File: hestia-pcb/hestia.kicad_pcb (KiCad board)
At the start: 4 copper layers, 90.2 x 95.9 mm, 181 parts, among them J1 Serial Connector, J12 B2B-ZR, J13 B2B-ZR, J14 B2B-ZR, J15 B2B-ZR, J16 B2B-ZR, J2 i2c connector, J3 ESQ-126-39-G-D, J4 ESQ-126-39-G-D, J5 VREF+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

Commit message: shift template designator/value locations for SRP5030C footprint in library. Update hestia PCB with SRP5030C footprint for L2 on buck regulator. change D7 footprint from SOT23 to smaller SOT-323 as per diode on BOM.
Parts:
- D7: footprint Package_TO_SOT_SMD:SOT-23 -> Package_TO_SOT_SMD:SOT-323_SC-70_Handsoldering
- L2: footprint Inductor_SMD:L_Coilcraft_LPS5030 -> Hestia:SRP5030C
- TH1, TH2, TH3, TH4, TH5, TH6: value Thermistor NTC 10K 3630K -> Thermistor NTC 10K 3610K
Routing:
- net +3.3V: track 114.3 -> 115.0 mm

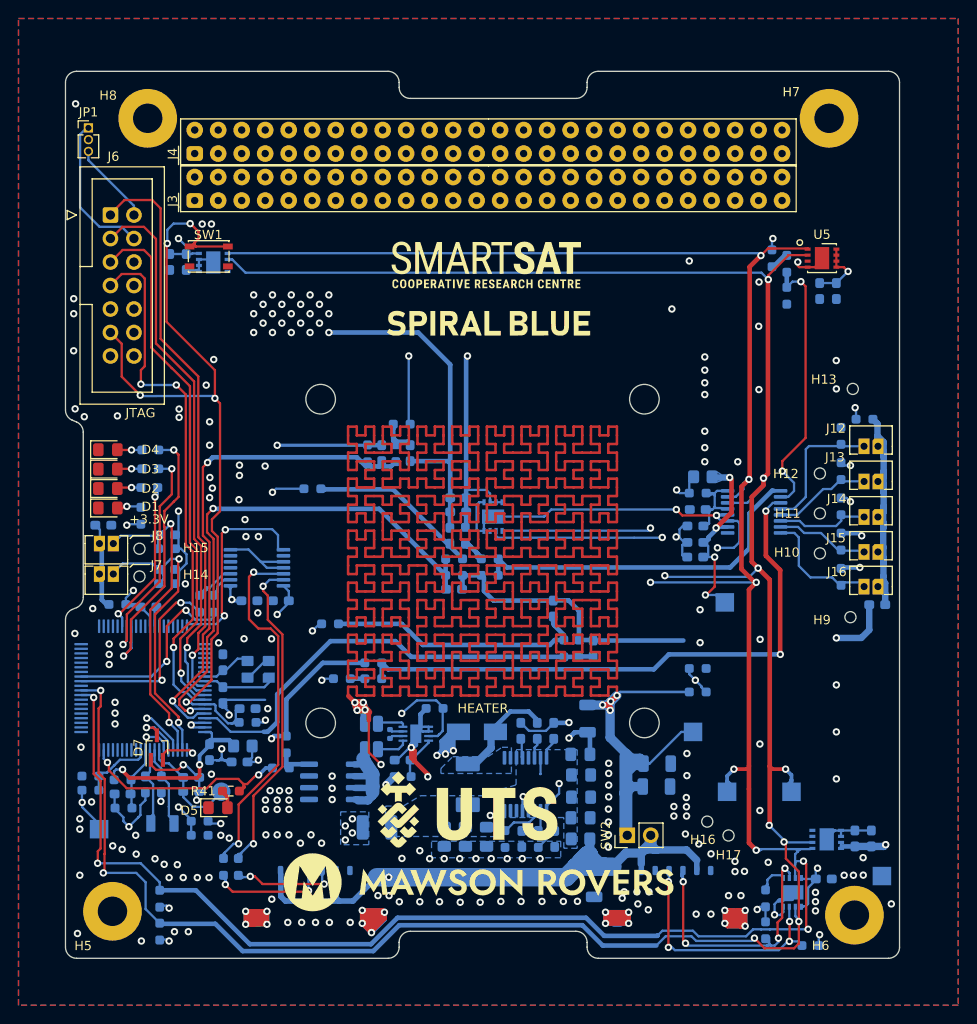
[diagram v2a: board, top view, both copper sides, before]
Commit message: added new themal switch footprint to hestia lib. Added 3 wire restraint hole footprints -> 1.2mm, 1.8mm and 1.9mm. Change adc wire restraint holes (H9 to H13) to 1.8mm. Change uC wire restraint holes(H14 & H15) to 1.8mm & moved H14 & H15 designators. Change thermal switch wire restraint holes (H16 & H17) to 1.9mm & also shifted hole coords left 0.2mm & moved H16 & H17 designators. Change thermal switch footprint to new footprint with thruhole pads to 1.2mm dia hole as well as with increased pad distance. Thicken VCC traces to thermal switch - have to revisit to satisfy DRC - probably change multiple traces to signal polygon. Added two GND vias for extra GND stitching off J2. ToDo -Resolve DRC issues. Some padd may need extra signal spurs to pads - just manually adding a trace to the pads may satisfy the DRC requirement
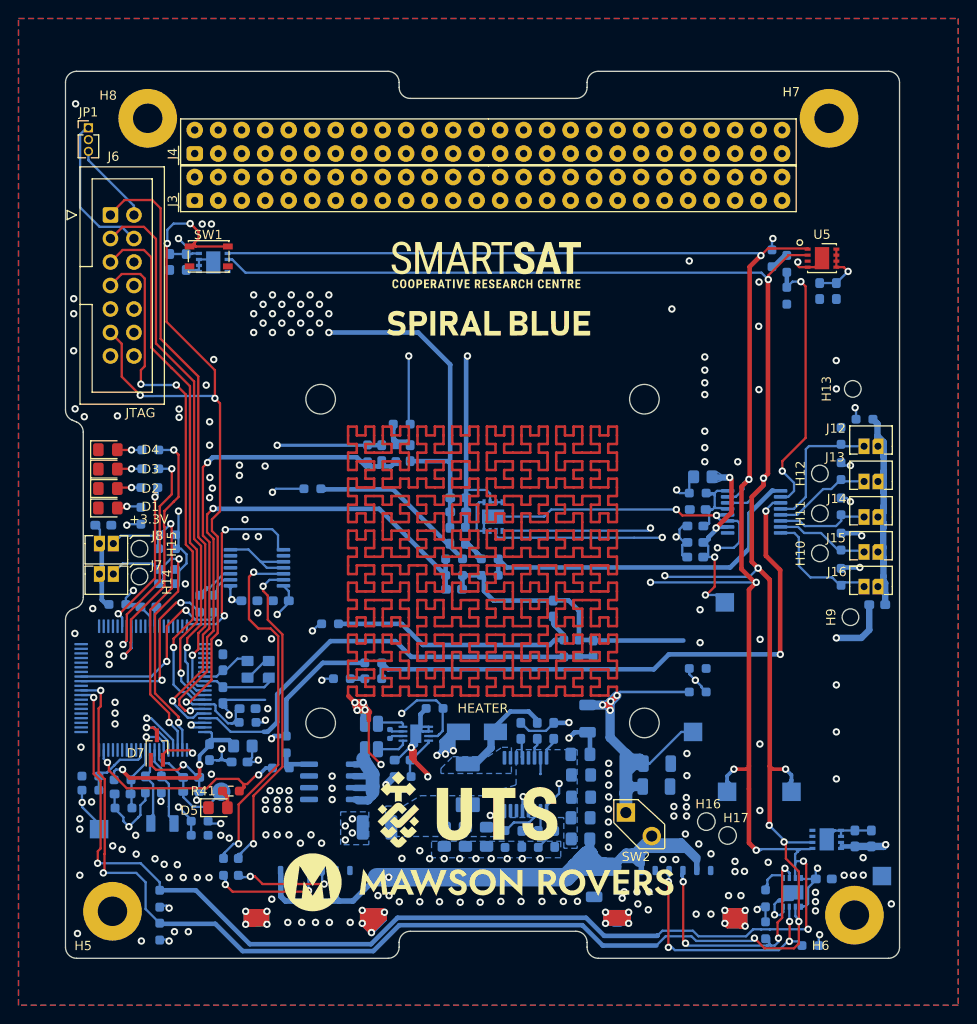
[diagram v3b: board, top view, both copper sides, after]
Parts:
- H10, H11, H12, H13, H14, H15, H9: footprint Hestia:Wire_Restraint_Hole -> Hestia:Wire_Restraint_Hole_1.8mm
- H16, H17: footprint Hestia:Wire_Restraint_Hole -> Hestia:Wire_Restraint_Hole_1.9mm
- SW2: footprint Connector_PinHeader_2.54mm:PinHeader_1x02_P2.54mm_Vertical -> Hestia:Thermal Switch
- moved SW2 2.46 mm to (162.2, 141.2), turned to 0 degrees
- moved H16 0.10 mm to (170.9, 142.2)
- moved H17 0.10 mm to (173.2, 143.7)
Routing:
- net VCC: track 94.3 -> 109.7 mm
- net /heater/Heater high: track 1006.0 -> 1003.4 mm
- net GND: vias 223 -> 225

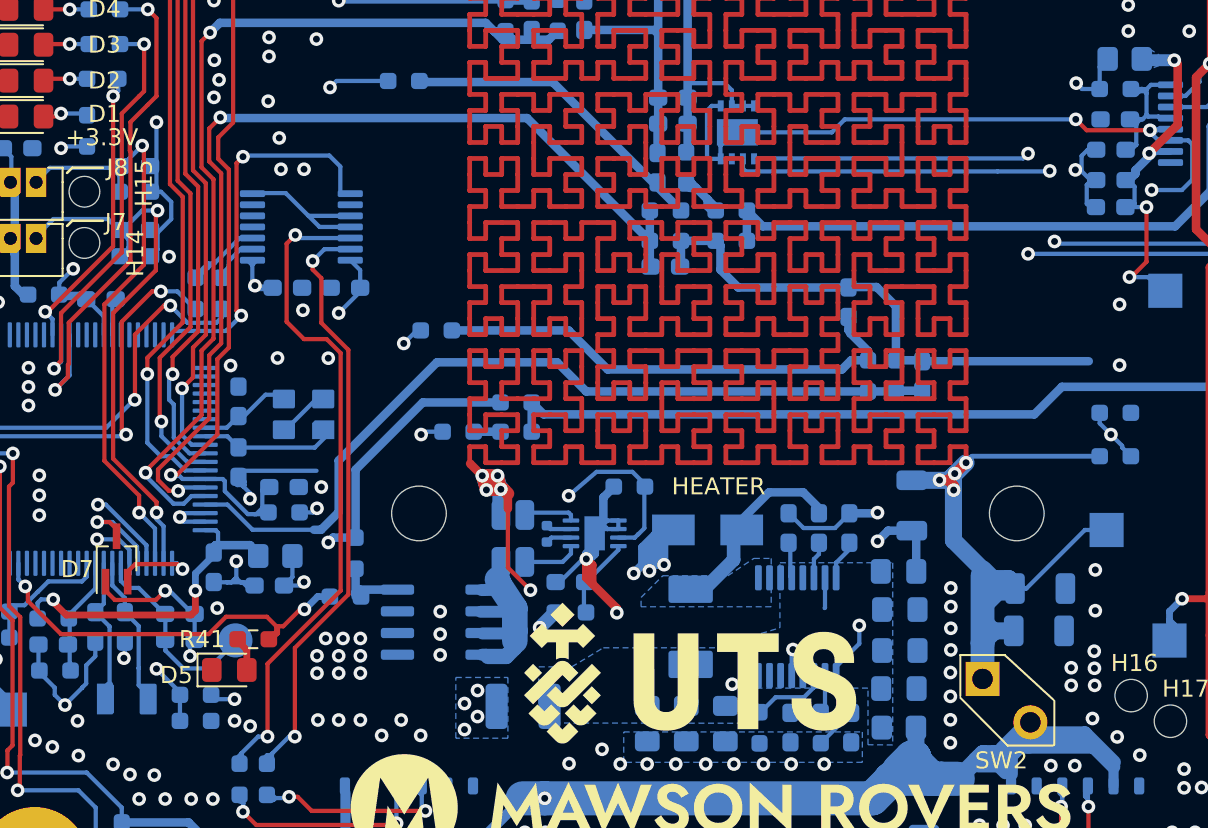
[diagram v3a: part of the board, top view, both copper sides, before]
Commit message: Moved U1 designator due to DRC violation. Moved C1 designator due to DRC violation after SW2 footprint was previously changed and shifted. Moved C26 designator due to DRC violation after SW2 footprint was previously changed and shifted. Changed R42 desgnator height to 0.8mm due to new DRC violation for minimum. Previous height was 0.6mm. Moved GND via near new thermal switch pads to satisfy DRC clearance violation. Move GND trace near D7 pin 2 to satisfy DRC clearance violation. Added PCB trace at C24 pin2 to satisfy ground polygon minimum thermal trace spoke to pad of 2 spokes.
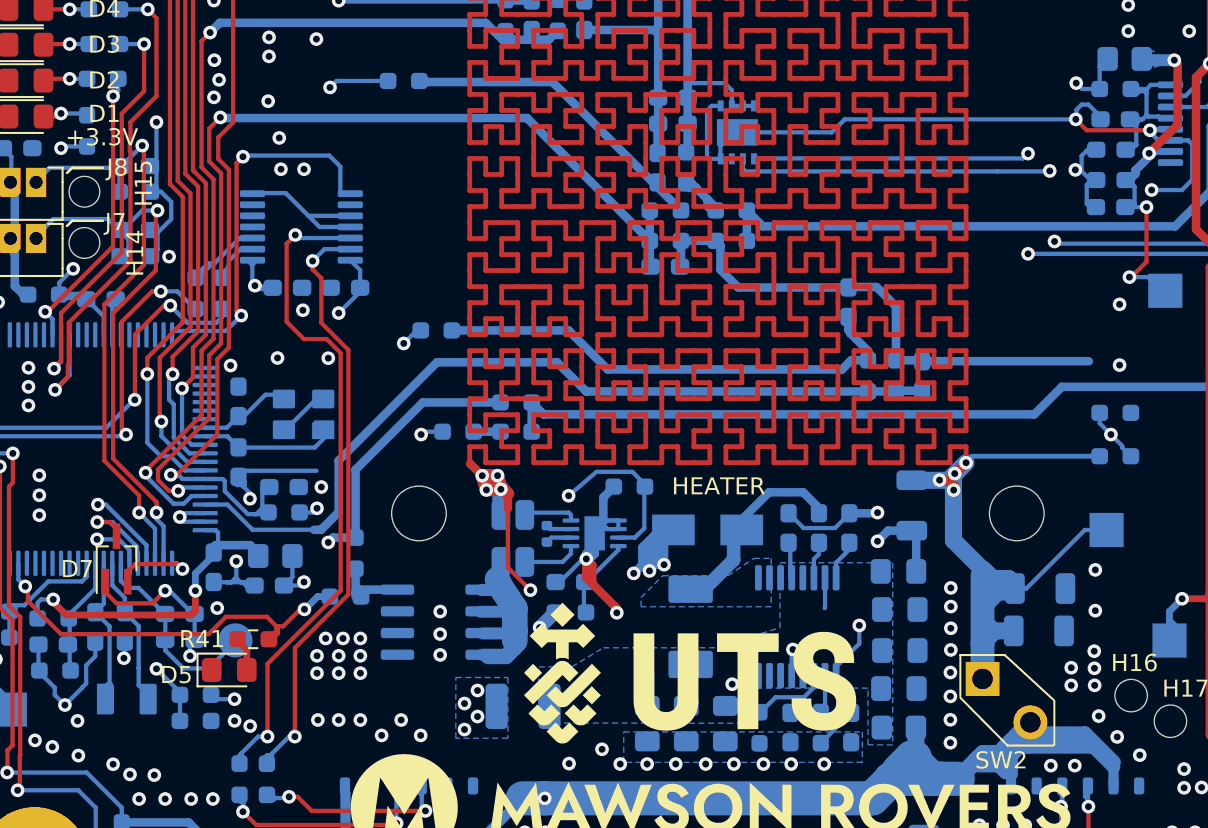
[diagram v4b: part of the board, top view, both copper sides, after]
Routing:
- net GND: track 282.2 -> 285.0 mm
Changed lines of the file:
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@@
     (property "ki_keywords" "cap capacitor")
     (attr smd)
-    (fp_text reference "C1" (at 4.5148 -0.0508) (layer "B.SilkS")
+    (fp_text reference "C1" (at 4.5148 1.2123) (layer "B.SilkS")
         (effects (font (size 1 1) (thickness 0.15)) (justify mirror))
     )
@@
     (property "ki_keywords" "cap capacitor")
     (attr smd)
-    (fp_text reference "C26" (at 4.677652 0.1686) (layer "B.SilkS")
+    (fp_text reference "C26" (at 4.677652 0.0383) (layer "B.SilkS")
         (effects (font (size 1 1) (thickness 0.15)) (justify mirror))
     )
@@
     (property "Type" "SMD")
     (attr smd)
-    (fp_text reference "U1" (at -3.090248 3.3518 -90) (layer "B.SilkS")
-        (effects (font (size 1 1) (thickness 0.15)) (justify mirror))
+    (fp_text reference "U1" (at -3.165248 3.3518 -90) (layer "B.SilkS")
+        (effects (font (size 0.8 0.8) (thickness 0.15)) (justify mirror))
     )
     (fp_text value "LM2655MTC-3.3/NOPB" (at 0 -3.45 90) (layer "B.Fab")
@@
     (attr smd)
     (fp_text reference "R42" (at 2.509116 -1.001059) (layer "B.SilkS")
-        (effects (font (size 0.6 0.6) (thickness 0.1)) (justify mirror))
+        (effects (font (size 0.8 0.8) (thickness 0.15) bold) (justify mirror))
     )
     (fp_text value "499R 0.1% 1/16W" (at 0 -1.16 90) (layer "B.Fab")
@@
   (gr_line (start 114.5814 118.2231) (end 115.2314 118.2231)
     (stroke (width 0.15) (type solid)) (layer "B.SilkS"))
-  (gr_line (start 160.9814 141.6231) (end 159.3314 141.6231)
-    (stroke (width 0.15) (type solid)) (layer "B.SilkS"))
   (gr_circle (center 181.9814 152.0231) (end 182.1314 152.1231)
     (stroke (width 0.15) (type solid)) (fill none) (layer "B.SilkS"))
@@
   (gr_line (start 115.216417 140.008421) (end 115.18482 139.713522)
     (stroke (width 0.15) (type solid)) (layer "B.SilkS"))
+  (gr_line (start 159.8814 142.9231) (end 160.9814 143.0231)
+    (stroke (width 0.15) (type default)) (layer "B.SilkS"))
   (gr_circle (center 126.3814 140.4231) (end 126.3814 140.1231)
     (stroke (width 0.15) (type solid)) (fill none) (layer "B.SilkS"))
@@
   (gr_line (start 160.4814 137.4731) (end 159.3814 137.4731)
     (stroke (width 0.15) (type solid)) (layer "B.SilkS"))
-  (gr_line (start 136.276671 130.6758) (end 136.613698 131.065488)
+  (gr_line (start 136.2814 130.7231) (end 136.613698 131.065488)
     (stroke (width 0.1) (type solid)) (layer "B.SilkS"))
   (gr_circle (center 181.3564 145.3731) (end 181.4814 145.5231)
@@
   (gr_line (start 136.613698 131.697414) (end 136.535813 131.615432)
     (stroke (width 0.1) (type solid)) (layer "B.SilkS"))
+  (gr_line (start 159.8814 142.9231) (end 159.3814 142.3231)
+    (stroke (width 0.15) (type default)) (layer "B.SilkS"))
   (gr_line (start 106.0577 140.0455) (end 106.0577 140.1852)
     (stroke (width 0.15) (type solid)) (layer "B.SilkS"))
@@
   (segment (start 168.2771 109.1231) (end 167.64 108.486) (width 0.25) (layer "F.Cu") (net 102))
   (segment (start 139.3314 135.6731) (end 138.9814 135.3231) (width 0.5) (layer "F.Cu") (net 102))
+  (segment (start 111.4814 136.8231) (end 113.5854 136.8231) (width 0.25) (layer "F.Cu") (net 102))
   (segment (start 181.838 82.283) (end 182.5977 82.283) (width 0.25) (layer "F.Cu") (net 102))
   (segment (start 140.769928 137.37548) (end 140.769928 137.111628) (width 0.5) (layer "F.Cu") (net 102))
+  (segment (start 110.7814 135.4106) (end 110.7814 136.1231) (width 0.25) (layer "F.Cu") (net 102))
   (segment (start 171.9814 109.1231) (end 168.2771 109.1231) (width 0.25) (layer "F.Cu") (net 102))
   (segment (start 183.4134 81.4673) (end 183.4134 81.3207) (width 0.25) (layer "F.Cu") (net 102))
   (segment (start 139.3314 134.5731) (end 139.3314 135.6731) (width 0.5) (layer "F.Cu") (net 102))
-  (segment (start 110.7814 135.4106) (end 110.7814 136.0231) (width 0.25) (layer "F.Cu") (net 102))
   (segment (start 138.9814 134.2231) (end 139.3314 134.5731) (width 0.5) (layer "F.Cu") (net 102))
   (segment (start 182.5977 82.283) (end 183.4134 81.4673) (width 0.25) (layer "F.Cu") (net 102))
-  (segment (start 111.3814 136.6231) (end 113.7854 136.6231) (width 0.25) (layer "F.Cu") (net 102))
   (segment (start 181.838 82.283) (end 180.9213 82.283) (width 0.25) (layer "F.Cu") (net 102))
   (segment (start 140.769928 137.111628) (end 139.3314 135.6731) (width 0.5) (layer "F.Cu") (net 102))
-  (segment (start 113.7854 136.6231) (end 114.3254 136.0831) (width 0.25) (layer "F.Cu") (net 102))
-  (segment (start 110.7814 136.0231) (end 111.3814 136.6231) (width 0.25) (layer "F.Cu") (net 102))
+  (segment (start 113.5854 136.8231) (end 114.3254 136.0831) (width 0.25) (layer "F.Cu") (net 102))
   (segment (start 180.9213 82.283) (end 180.7718 82.1335) (width 0.25) (layer "F.Cu") (net 102))
+  (segment (start 110.7814 136.1231) (end 111.4814 136.8231) (width 0.25) (layer "F.Cu") (net 102))
   (segment (start 180.7718 82.1335) (end 180.7718 81.7271) (width 0.25) (layer "F.Cu") (net 102))
   (segment (start 138.9814 135.3231) (end 138.9814 134.2231) (width 0.5) (layer "F.Cu") (net 102))
@@
   (via (at 156.0322 131.5111) (size 0.8) (drill 0.4) (layers "F.Cu" "B.Cu") (free) (net 102))
   (via (at 184.9374 122.3671) (size 0.8) (drill 0.4) (layers "F.Cu" "B.Cu") (free) (net 102))
-  (via (at 168.6179 143.5634) (size 0.8) (drill 0.4) (layers "F.Cu" "B.Cu") (free) (net 102))
+  (via (at 168.9814 143.4231) (size 0.8) (drill 0.4) (layers "F.Cu" "B.Cu") (free) (net 102))
   (via (at 169.037 81.6128) (size 0.8) (drill 0.4) (layers "F.Cu" "B.Cu") (free) (net 102))
   (via (at 103.1494 141.9251) (size 0.8) (drill 0.4) (layers "F.Cu" "B.Cu") (free) (net 102))
@@
   (segment (start 139.4714 132.7231) (end 139.9814 132.2131) (width 0.25) (layer "B.Cu") (net 102))
   (segment (start 142.2654 134.5591) (end 143.5354 134.5591) (width 0.5) (layer "B.Cu") (net 102))
+  (segment (start 169.0889 108.486) (end 169.0889 108.3306) (width 0.25) (layer "B.Cu") (net 102))
   (segment (start 143.1544 108.776266) (end 143.190666 108.74) (width 0.5) (layer "B.Cu") (net 102))
   (segment (start 143.0814 133.3631) (end 143.7214 132.7231) (width 0.5) (layer "B.Cu") (net 102))
@@
   (segment (start 155.9814 118.3031) (end 154.3569 118.3031) (width 0.5) (layer "B.Cu") (net 102))
   (segment (start 178.7814 150.6231) (end 180.2064 150.6231) (width 0.25) (layer "B.Cu") (net 102))
+  (segment (start 169.0889 108.3306) (end 168.3814 107.6231) (width 0.25) (layer "B.Cu") (net 102))
   (segment (start 188.722 143.1835) (end 186.944 143.1835) (width 0.25) (layer "B.Cu") (net 102))
   (segment (start 111.3525 119.11) (end 111.232 119.2305) (width 0.25) (layer "B.Cu") (net 102))
@@
   (segment (start 168.3405 110.264) (end 167.9814 110.6231) (width 0.25) (layer "B.Cu") (net 102))
   (segment (start 114.6814 114.3231) (end 114.6814 113.3231) (width 0.25) (layer "B.Cu") (net 102))
+  (segment (start 167.9814 107.6231) (end 167.6814 107.9231) (width 0.25) (layer "B.Cu") (net 102))
   (segment (start 151.0082 139.5958) (end 151.0792 139.5248) (width 0.25) (layer "B.Cu") (net 102))
   (segment (start 158.0388 132.567) (end 156.6527 132.567) (width 0.5) (layer "B.Cu") (net 102))
@@
   (segment (start 106.9086 140.8075) (end 107.8611 141.76) (width 0.25) (layer "B.Cu") (net 102))
   (segment (start 144.526 117.0574) (end 144.4741 117.1093) (width 0.5) (layer "B.Cu") (net 102))
+  (segment (start 167.6814 107.9231) (end 167.6814 108.5231) (width 0.25) (layer "B.Cu") (net 102))
   (segment (start 184.6326 143.1951) (end 184.785 143.1951) (width 0.25) (layer "B.Cu") (net 102))
   (segment (start 167.9814 110.6231) (end 167.9814 111.5231) (width 0.25) (layer "B.Cu") (net 102))
@@
   (segment (start 153.3525 109.248) (end 154.1145 108.486) (width 0.25) (layer "B.Cu") (net 102))
   (segment (start 142.2654 134.5591) (end 142.2654 133.5431) (width 0.5) (layer "B.Cu") (net 102))
+  (segment (start 168.3814 107.6231) (end 167.9814 107.6231) (width 0.25) (layer "B.Cu") (net 102))
   (segment (start 140.8589 131.9731) (end 140.2214 131.9731) (width 0.25) (layer "B.Cu") (net 102))
   (segment (start 137.1884 135.5751) (end 137.4294 135.5751) (width 0.25) (layer "B.Cu") (net 102))
